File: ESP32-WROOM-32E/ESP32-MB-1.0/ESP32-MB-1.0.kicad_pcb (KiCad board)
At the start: 2 copper layers, 125.6 x 91.4 mm, 52 parts, among them J1 Conn_01x19, J10 Conn_01x03_Pin, J11 Conn_01x03_Pin, J12 Conn_01x03_Pin, J13 Conn_01x03_Pin, J14 Conn_01x03_Pin, J15 Conn_01x03_Pin, J16 XT60-M, J2 Conn_01x19, J21 Conn_01x02_Pin, J22 XT60-M, J23 Conn_01x02_Pin, J24 Conn_01x02_Pin, J25 Conn_01x02_Pin, J26 Conn_01x02_Pin, J27 Conn_01x02_Pin, J28 Conn_01x02_Pin, J29 Conn_01x02_Pin, J3 Conn_01x19, J30 XT60-M, J31 Conn_01x02_Pin, J32 Conn_01x02_Pin, J33 Conn_01x11_Pin, J34 Conn_01x02_Pin, J35 Conn_01x02_Pin, J36 Conn_01x02_Pin, J37 Conn_01x02_Pin, J38 Conn_01x02_Pin, J39 Conn_01x02_Pin, J4 Conn_01x11_Pin, J5 Conn_01x11_Pin, J6 XT60-M, J7 Conn_01x19, J8 Conn_01x03_Pin, J9 Conn_01x03_Pin, U1 IRLB3813PBF, U2 IRLB3813PBF, U3 IRLB3813PBF, U4 IRLB3813PBF, U5 IRLB3813PBF, U6 IRLB3813PBF, U7 IRLB3813PBF, U8 IRLB3813PBF, U9 MCP2562-E-P

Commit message: 100になれなかったモタドラ4枚
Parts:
- added J4: Conn_01x11_Pin, Connector_PinHeader_2.54mm:PinHeader_1x11_P2.54mm_Vertical, F.Cu at (134.0, 103.3)
- moved J26 93.7 mm to (234.0, 125.9), turned to 90 degrees
- moved J21 90.7 mm to (227.3, 125.9), turned to 90 degrees
- moved J6 25.8 mm to (158.0, 127.6), turned to 180 degrees
- moved J22 18.4 mm to (158.1, 109.1), turned to 180 degrees
- moved J16 12.8 mm to (157.8, 99.7), turned to 180 degrees
- moved J23 8.94 mm to (142.0, 61.6)
- moved J28 8.94 mm to (142.2, 75.3)
- moved J25 8.94 mm to (142.0, 54.9)
- moved J27 8.94 mm to (142.2, 68.5)
- moved J29 8.94 mm to (141.9, 48.6)
- moved J24 8.94 mm to (142.2, 82.1)
- moved J30 5.93 mm to (158.3, 118.3), turned to 180 degrees
- moved J31 1.67 mm to (199.7, 126.1)
- moved J32 1.67 mm to (206.6, 126.1)
- moved J34 1.67 mm to (213.3, 126.0)
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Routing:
- net +_servo: track 0.00 -> 128.9 mm
- net GND: track 0.00 -> 128.2 mm
- net 24V_IN: track 0.00 -> 67.6 mm
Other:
- board size 125.6 x 91.4 mm -> 116.1 x 97.9 mm

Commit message: １００×１００
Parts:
- R1, R2, R3, R4, R5, R6, R7, R8, U9: moved to B.Cu
- moved J26 133.1 mm to (106.9, 86.2), turned to 0 degrees
- moved J21 129.0 mm to (106.9, 79.5), turned to 0 degrees
- moved J35 115.2 mm to (109.4, 94.1), turned to 180 degrees
- moved J34 106.7 mm to (109.6, 101.0), turned to 180 degrees
- moved J32 98.6 mm to (109.6, 107.7), turned to 180 degrees
- moved J31 90.8 mm to (109.7, 114.6), turned to 180 degrees
- moved J1 85.1 mm to (95.3, 82.2), turned to 0 degrees
- moved U3 84.1 mm to (152.0, 82.0)
- moved U4 84.1 mm to (152.0, 92.1)
- moved U7 84.1 mm to (152.0, 76.9)
- moved U8 84.1 mm to (152.0, 87.0)
- moved U1 83.9 mm to (151.8, 46.6)
- moved U2 83.9 mm to (151.8, 56.8)
- moved U5 83.9 mm to (151.8, 51.7)
- moved U6 83.9 mm to (151.8, 61.9)
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- renumbered J4 to J17
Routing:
- net GND: track 128.2 -> 220.0 mm
- net 24V_IN: track 67.6 -> 94.7 mm
- net +_servo: track 128.9 -> 143.7 mm
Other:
- board outline removed

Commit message: モタドラ４つT完成　田代先輩確認お願いします
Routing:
- net GND: track 220.0 -> 537.5 mm, vias 0 -> 2
- net 0_GPIO13: track 0.00 -> 187.3 mm, vias 0 -> 1
- net 0_GPIO27: track 0.00 -> 186.6 mm, vias 0 -> 2
- net 0_GPIO12: track 0.00 -> 183.4 mm, vias 0 -> 2
- net 0_GPIO14: track 0.00 -> 164.8 mm, vias 0 -> 1
- net 1_GPIO13: track 0.00 -> 164.2 mm, vias 0 -> 1
- net 1_GPIO12: track 0.00 -> 154.3 mm, vias 0 -> 3
- net 0_+5V: track 0.00 -> 145.3 mm, vias 0 -> 1
- net 0_GPIO33: track 0.00 -> 140.6 mm, vias 0 -> 2
- net 1_GPIO16: track 0.00 -> 133.0 mm, vias 0 -> 1
- net 1_GPIO2: track 0.00 -> 130.3 mm, vias 0 -> 1
- net 0_GPIO32: track 0.00 -> 129.6 mm, vias 0 -> 2
- net 0_GPIO5: track 0.00 -> 128.5 mm, vias 0 -> 2
- net Net-(J31-Pin_1): track 0.00 -> 127.1 mm
- net 1_GPIO5: track 0.00 -> 121.9 mm, vias 0 -> 1
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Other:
- board outline added: 118.6 x 123.4 mm

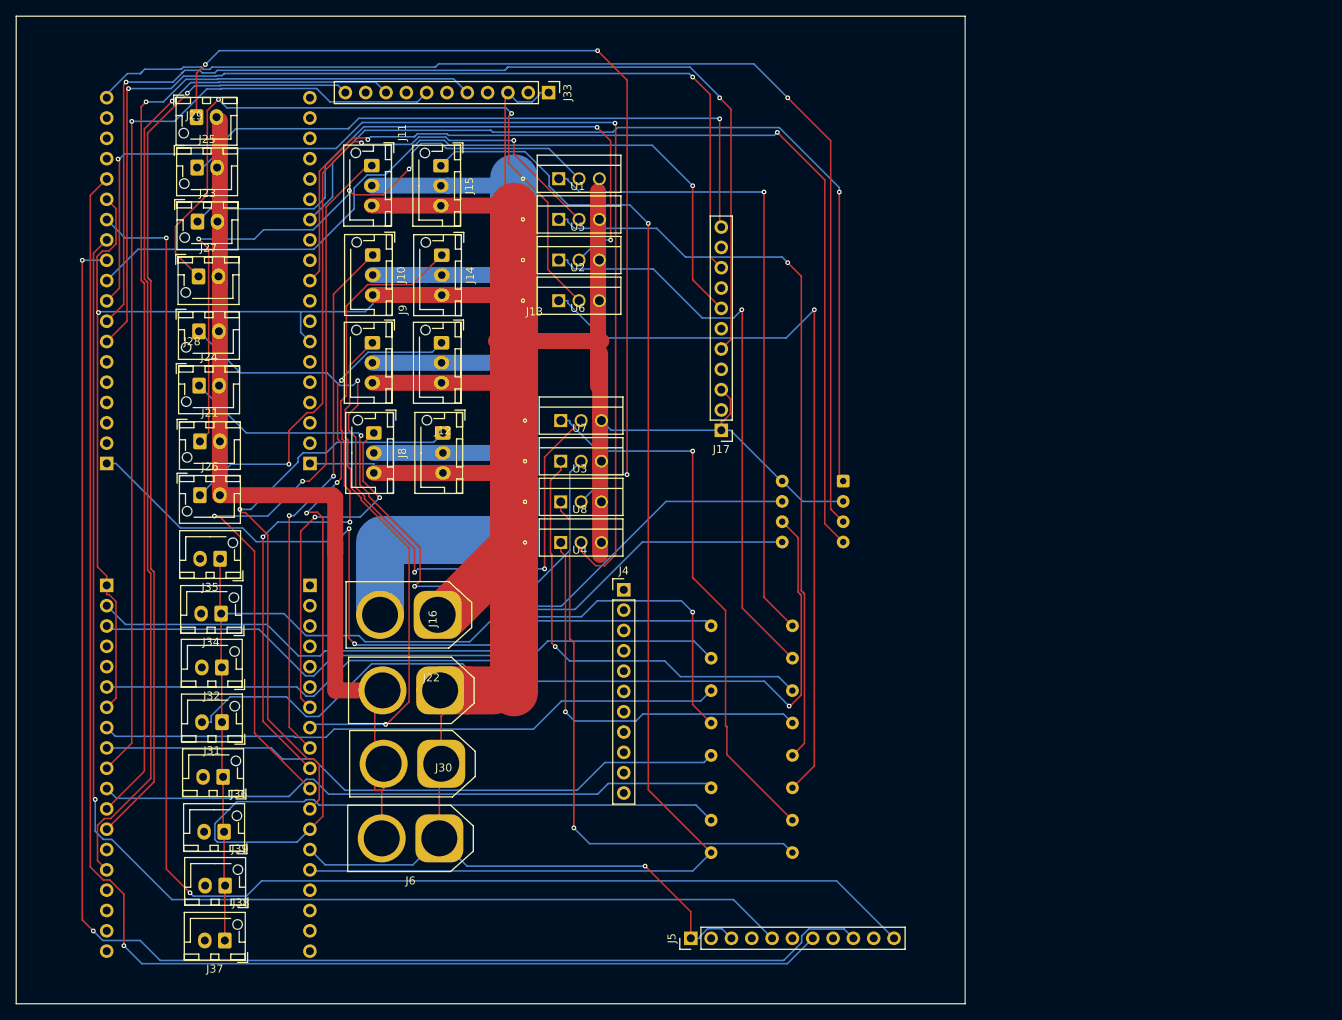
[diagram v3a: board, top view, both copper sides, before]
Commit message: 配線変更
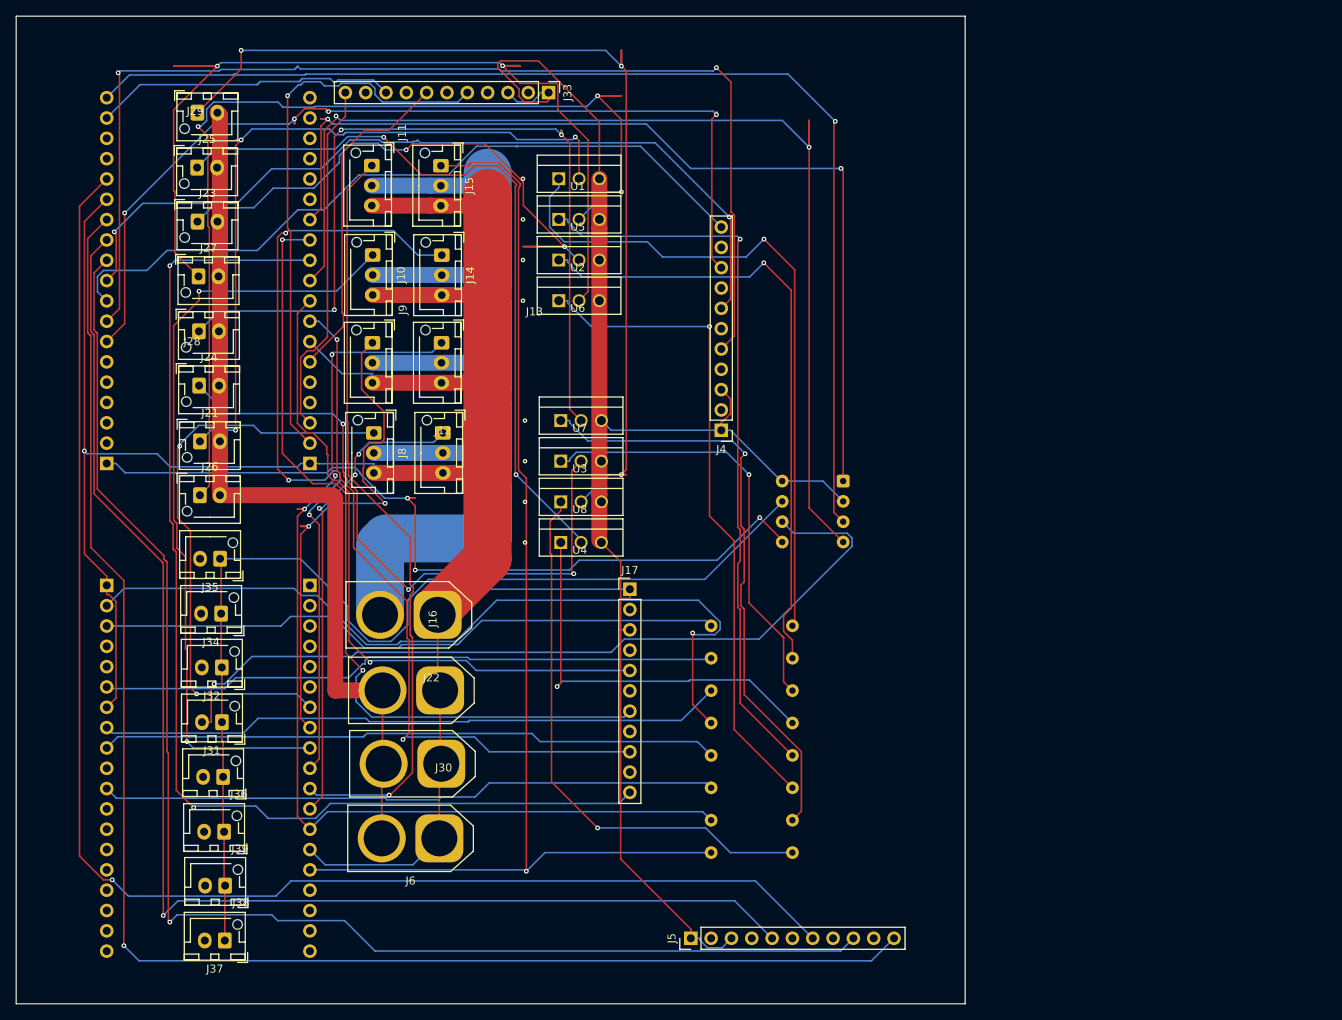
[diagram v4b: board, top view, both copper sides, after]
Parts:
- removed the J4 at (159.9, 98.0)
- added J17: Conn_01x11_Pin, Connector_PinHeader_2.54mm:PinHeader_1x11_P2.54mm_Vertical, F.Cu at (160.7, 98.0)
- moved J29 0.56 mm to (106.6, 38.4)
- renumbered J17 to J4
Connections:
- net 1_GZPIO3 renamed 1_GPIO3
- J33 pad 11: 1_GPIO4 -> 0_GPIO22
- J33 pad 5: 1_GPIO16 -> 0_GPIO23
- J33 pad 7: 1_GPIO5 -> 0_GPIO21
- J33 pad 9: 1_GPIO2 -> 0_GPIO11
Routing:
- net 0_GPIO17: track 0.00 -> 143.7 mm, vias 0 -> 2
- net 1_GPIO16: track 133.0 -> 0.00 mm, vias 1 -> 0
- net 1_GPIO2: track 130.3 -> 0.00 mm, vias 1 -> 0
- net 1_GPIO5: track 121.9 -> 0.00 mm, vias 1 -> 0
- net 1_GPIO4: track 117.8 -> 0.00 mm, vias 1 -> 0
- net 0_GPIO16: track 0.00 -> 102.8 mm, vias 0 -> 2
- net 0_GPIO19: track 0.00 -> 87.9 mm, vias 0 -> 2
- net 0_GPIO18: track 0.00 -> 83.6 mm, vias 0 -> 1
- net 0_GPIO23: track 0.00 -> 70.3 mm, vias 0 -> 1
- net 0_GPIO22: track 0.00 -> 44.5 mm
- net Net-(J27-Pin_1): track 90.1 -> 133.7 mm
- net Net-(J26-Pin_1): track 90.8 -> 133.2 mm
- net 0_GPIO21: track 0.00 -> 41.8 mm
- net 0_GPIO11: track 0.00 -> 38.7 mm
- net 1_GPIO25: track 67.4 -> 98.2 mm
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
